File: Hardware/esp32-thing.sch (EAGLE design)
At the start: 70 parts, among them Q1 2.5A/30V, Q2 MBT3904DW1T1, U1 MCP73831, U2 ESP31B, U3 AP2112K-3.3V, U4 FT231XS, U5 W25Q32FVSS, Y1 26MHz, Y2 32.768kHz

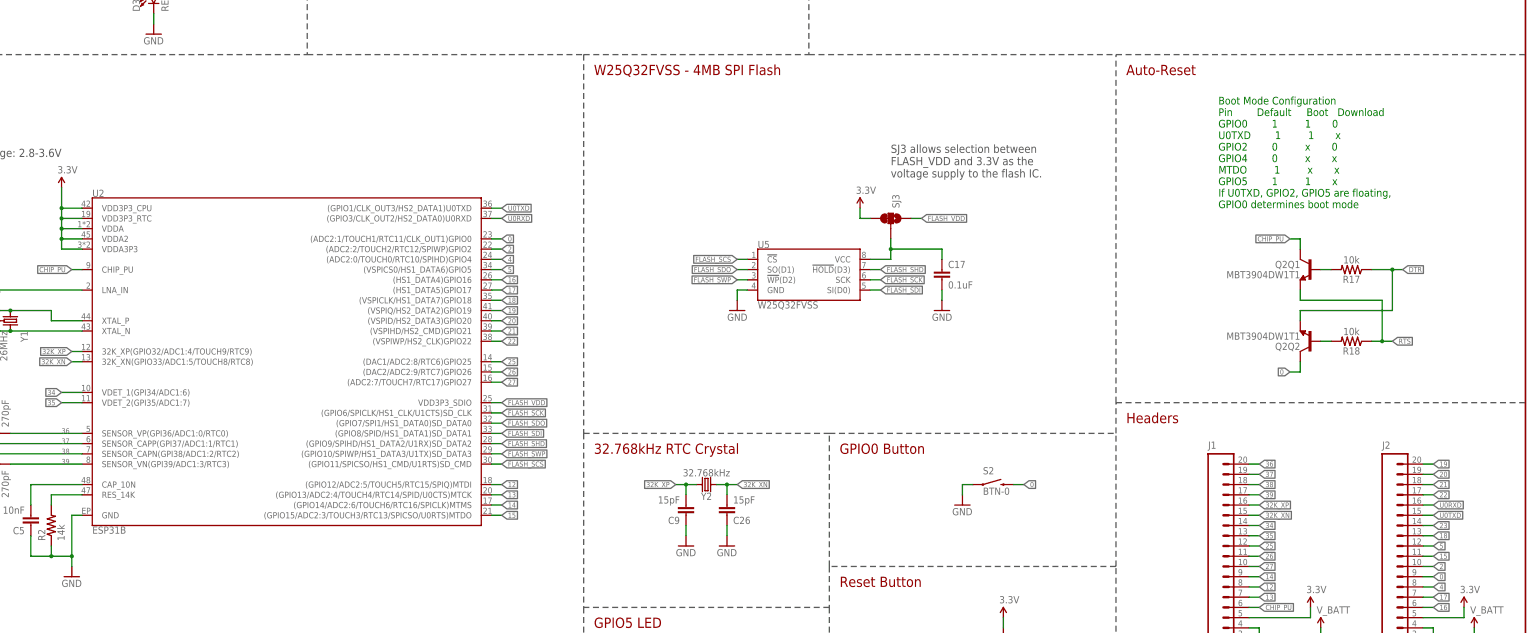
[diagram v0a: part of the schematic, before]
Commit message: Swapping ESP32 in for ESP31B, adding pull-up to GPIO0
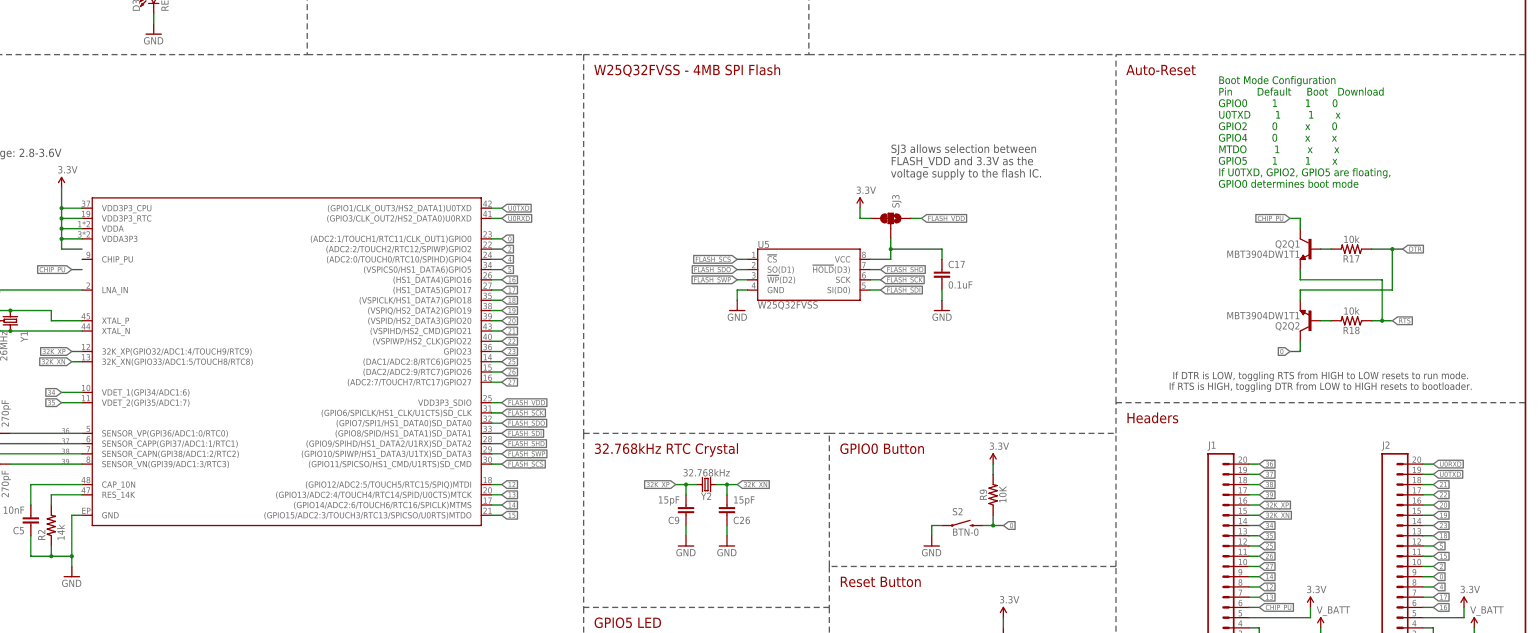
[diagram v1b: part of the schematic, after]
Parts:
- removed U2: ESP31B, esp32-thing-temp:ESP31B
- added R9: 10K, SparkFun-Resistors:10KOHM-1/10W-1%(0603)0603
- added U$1: ESP32, esp32-thing-temp:ESP32
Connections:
- net 0: now also R9.1, U$1.(ADC2:1/TOUCH1/RTC11/CLK_OUT1)GPIO0; no longer U2.(ADC2:1/TOUCH1/RTC11/CLK_OUT1)GPIO0
- net 12: now also U$1.(GPIO12/ADC2:5/TOUCH5/RTC15/SPIQ)MTDI; no longer U2.(GPIO12/ADC2:5/TOUCH5/RTC15/SPIQ)MTDI
- net 13: now also U$1.(GPIO13/ADC2:4/TOUCH4/RTC14/SPID/U0CTS)MTCK; no longer U2.(GPIO13/ADC2:4/TOUCH4/RTC14/SPID/U0CTS)MTCK
- net 14: now also U$1.(GPIO14/ADC2:6/TOUCH6/RTC16/SPICLK)MTMS; no longer U2.(GPIO14/ADC2:6/TOUCH6/RTC16/SPICLK)MTMS
- net 15: now also U$1.(GPIO15/ADC2:3/TOUCH3/RTC13/SPICSO/U0RTS)MTDO; no longer U2.(GPIO15/ADC2:3/TOUCH3/RTC13/SPICSO/U0RTS)MTDO
- net 16: now also U$1.(HS1_DATA4)GPIO16; no longer U2.(HS1_DATA4)GPIO16
- net 17: now also U$1.(HS1_DATA5)GPIO17; no longer U2.(HS1_DATA5)GPIO17
- net 18: now also U$1.(VSPICLK/HS1_DATA7)GPIO18; no longer U2.(VSPICLK/HS1_DATA7)GPIO18
- net 19: now also J2.15, U$1.(VSPIQ/HS2_DATA2)GPIO19; no longer J2.20, U2.(VSPIQ/HS2_DATA2)GPIO19
- net 2: now also U$1.(ADC2:2/TOUCH2/RTC12/SPIWP)GPIO2; no longer U2.(ADC2:2/TOUCH2/RTC12/SPIWP)GPIO2
- net 20: now also J2.16, U$1.(VSPID/HS2_DATA3)GPIO20; no longer J2.19, U2.(VSPID/HS2_DATA3)GPIO20
- net 21: now also U$1.(VSPIHD/HS2_CMD)GPIO21; no longer U2.(VSPIHD/HS2_CMD)GPIO21
- net 22: now also U$1.(VSPIWP/HS2_CLK)GPIO22; no longer U2.(VSPIWP/HS2_CLK)GPIO22
- net 23: now also U$1.GPIO23
- net 25: now also U$1.(DAC1/ADC2:8/RTC6)GPIO25; no longer U2.(DAC1/ADC2:8/RTC6)GPIO25
- net 26: now also U$1.(DAC2/ADC2:9/RTC7)GPIO26; no longer U2.(DAC2/ADC2:9/RTC7)GPIO26
- net 27: now also U$1.(ADC2:7/TOUCH7/RTC17)GPIO27; no longer U2.(ADC2:7/TOUCH7/RTC17)GPIO27
- net 3.3V: now also R9.2, U$1.VDD3P3_CPU, U$1.VDD3P3_RTC, U$1.VDDA, U$1.VDDA3P3; no longer U2.VDD3P3_CPU, U2.VDD3P3_RTC, U2.VDDA, U2.VDDA2, U2.VDDA3P3
- net 32K_XN: now also U$1.32K_XN(GPIO33/ADC1:5/TOUCH8/RTC8); no longer U2.32K_XN(GPIO33/ADC1:5/TOUCH8/RTC8)
- net 32K_XP: now also U$1.32K_XP(GPIO32/ADC1:4/TOUCH9/RTC9); no longer U2.32K_XP(GPIO32/ADC1:4/TOUCH9/RTC9)
- net 34: now also U$1.VDET_1(GPI34/ADC1:6); no longer U2.VDET_1(GPI34/ADC1:6)
- net 35: now also U$1.VDET_2(GPI35/ADC1:7); no longer U2.VDET_2(GPI35/ADC1:7)
- net 36: now also U$1.SENSOR_VP(GPI36/ADC1:0/RTC0); no longer U2.SENSOR_VP(GPI36/ADC1:0/RTC0)
- net 37: now also U$1.SENSOR_CAPP(GPI37/ADC1:1/RTC1); no longer U2.SENSOR_CAPP(GPI37/ADC1:1/RTC1)
- net 38: now also U$1.SENSOR_CAPN(GPI38/ADC1:2/RTC2); no longer U2.SENSOR_CAPN(GPI38/ADC1:2/RTC2)
- net 39: now also U$1.SENSOR_VN(GPI39/ADC1:3/RTC3); no longer U2.SENSOR_VN(GPI39/ADC1:3/RTC3)
- net 4: now also U$1.(ADC2:0/TOUCH0/RTC10/SPIHD)GPIO4; no longer U2.(ADC2:0/TOUCH0/RTC10/SPIHD)GPIO4
- net 5: now also U$1.(VSPICS0/HS1_DATA6)GPIO5; no longer U2.(VSPICS0/HS1_DATA6)GPIO5
- net CAP_10N: now also U$1.CAP_10N; no longer U2.CAP_10N
- net CHIP_PU: no longer U2.CHIP_PU
- net FLASH_SCK: now also U$1.(GPIO6/SPICLK/HS1_CLK/U1CTS)SD_CLK; no longer U2.(GPIO6/SPICLK/HS1_CLK/U1CTS)SD_CLK
- net FLASH_SCS: now also U$1.(GPIO11/SPICSO/HS1_CMD/U1RTS)SD_CMD; no longer U2.(GPIO11/SPICSO/HS1_CMD/U1RTS)SD_CMD
- net FLASH_SDI: now also U$1.(GPIO8/SPID/HS1_DATA1)SD_DATA1; no longer U2.(GPIO8/SPID/HS1_DATA1)SD_DATA1
- net FLASH_SDO: now also U$1.(GPIO7/SPI1/HS1_DATA0)SD_DATA0; no longer U2.(GPIO7/SPI1/HS1_DATA0)SD_DATA0
- net FLASH_SHD: now also U$1.(GPIO9/SPIHD/HS1_DATA2/U1RX)SD_DATA2; no longer U2.(GPIO9/SPIHD/HS1_DATA2/U1RX)SD_DATA2
- net FLASH_SWP: now also U$1.(GPIO10/SPIWP/HS1_DATA3/U1TX)SD_DATA3; no longer U2.(GPIO10/SPIWP/HS1_DATA3/U1TX)SD_DATA3
- net FLASH_VDD: now also U$1.VDD3P3_SDIO; no longer U2.VDD3P3_SDIO
- net GND: now also U$1.GND; no longer U2.GND
- net LNA_IN: now also U$1.LNA_IN; no longer U2.LNA_IN
- net N$13: now also U$1.XTAL_P; no longer U2.XTAL_P
- net N$15: now also U$1.XTAL_N; no longer U2.XTAL_N
- net RES_14K: now also U$1.RES_14K; no longer U2.RES_14K
- net U0RXD: now also J2.20, U$1.(GPIO3/CLK_OUT2/HS2_DATA0)U0RXD; no longer J2.16, U2.(GPIO3/CLK_OUT2/HS2_DATA0)U0RXD
- net U0TXD: now also J2.19, U$1.(GPIO1/CLK_OUT3/HS2_DATA1)U0TXD; no longer J2.15, U2.(GPIO1/CLK_OUT3/HS2_DATA1)U0TXD
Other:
- note added: "If DTR is LOW, toggling RTS from HIGH to LOW resets to run mode. If RTS is HIGH, toggling DTR from LOW to HIGH resets to bootloader."
- moved on the sheet: Q2Q1, Q2Q2, R17, R18, S2

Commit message: Fixing reset pin wiring.
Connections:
- net CHIP_PU: now also U$1.CHIP_PU
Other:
- note added: "v02"
- note removed: "v01"
- moved on the sheet: C1, C2, J1, J2
